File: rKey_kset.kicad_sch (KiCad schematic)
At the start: 25 parts, among them J1 Conn_01x08, Q1 BC337, Q2 BC337, Q3 BC337, Q4 BC337, Q5 BC337, Q6 BC337

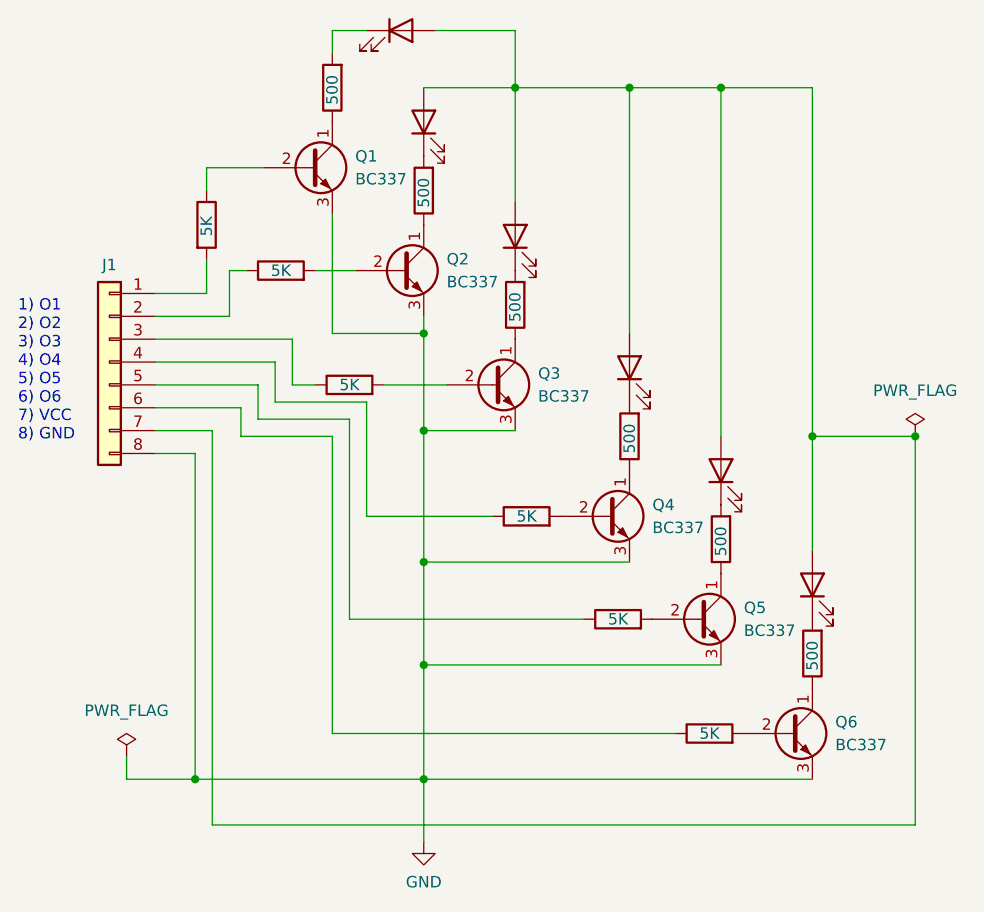
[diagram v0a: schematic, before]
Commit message: change: resistors values tuned to reduce the required current
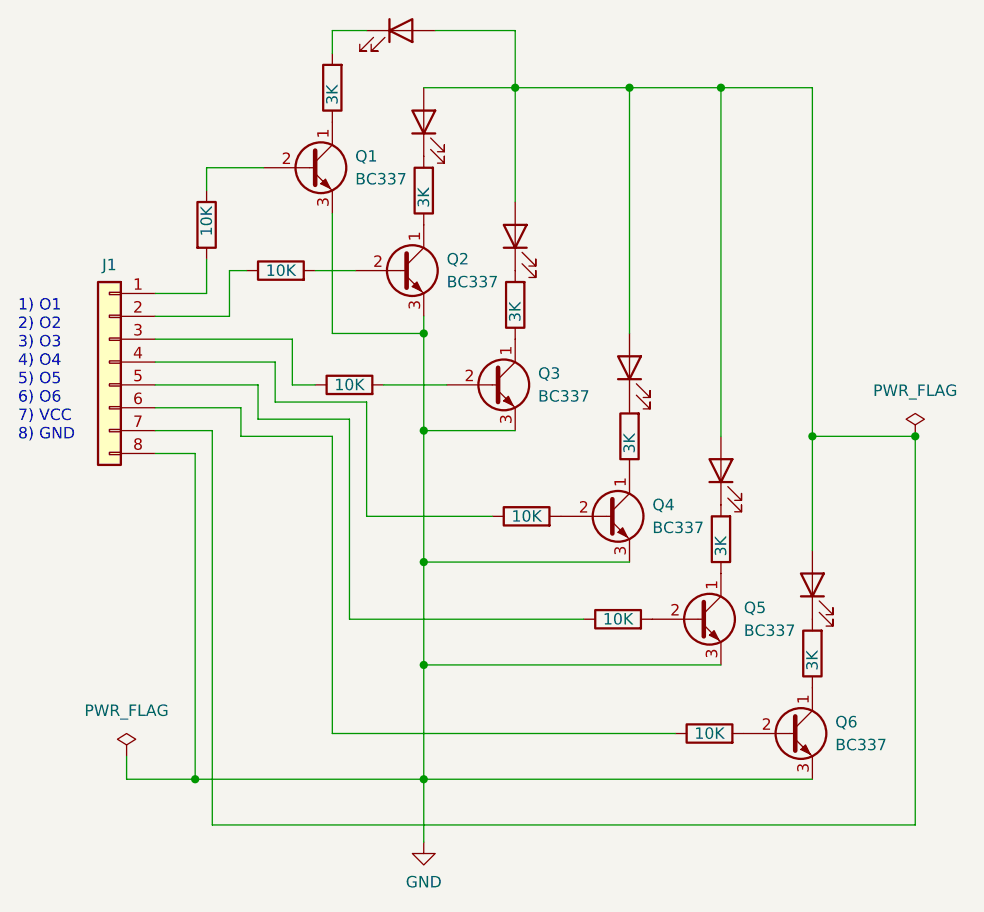
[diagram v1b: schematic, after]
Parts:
- R1, R10, R2, R4, R7, R8: value 5K -> 10K
- R11, R12, R3, R5, R6, R9: value 500 -> 3K
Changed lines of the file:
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@@
       (effects (font (size 1.27 1.27)) (justify right) hide)
     )
-    (property "Value" "500" (id 1) (at 160.655 114.3 90)
+    (property "Value" "3K" (id 1) (at 160.655 114.3 90)
       (effects (font (size 1.27 1.27)) (justify right))
     )
@@
       (effects (font (size 1.27 1.27)) (justify right) hide)
     )
-    (property "Value" "500" (id 1) (at 127.635 75.565 90)
+    (property "Value" "3K" (id 1) (at 127.635 75.565 90)
       (effects (font (size 1.27 1.27)) (justify right))
     )
@@
       (effects (font (size 1.27 1.27)) (justify right) hide)
     )
-    (property "Value" "500" (id 1) (at 117.475 62.865 90)
+    (property "Value" "3K" (id 1) (at 117.475 62.865 90)
       (effects (font (size 1.27 1.27)) (justify right))
     )
@@
       (effects (font (size 1.27 1.27)) hide)
     )
-    (property "Value" "5K" (id 1) (at 149.225 121.285 90))
+    (property "Value" "10K" (id 1) (at 149.225 121.285 90))
     (property "Footprint" "Resistor_THT:R_Axial_DIN0207_L6.3mm_D2.5mm_P7.62mm_Horizontal" (id 2) (at 149.225 123.063 90)
       (effects (font (size 1.27 1.27)) hide)
@@
       (effects (font (size 1.27 1.27)) (justify left) hide)
     )
-    (property "Value" "5K" (id 1) (at 93.345 66.04 90)
+    (property "Value" "10K" (id 1) (at 93.345 66.04 90)
       (effects (font (size 1.27 1.27)) (justify left))
     )
@@
       (effects (font (size 1.27 1.27)) (justify right) hide)
     )
-    (property "Value" "500" (id 1) (at 150.495 101.6 90)
+    (property "Value" "3K" (id 1) (at 150.495 101.6 90)
       (effects (font (size 1.27 1.27)) (justify right))
     )
@@
       (effects (font (size 1.27 1.27)) (justify right) hide)
     )
-    (property "Value" "500" (id 1) (at 140.335 90.17 90)
+    (property "Value" "3K" (id 1) (at 140.335 90.17 90)
       (effects (font (size 1.27 1.27)) (justify right))
     )
@@
       (effects (font (size 1.27 1.27)) hide)
     )
-    (property "Value" "5K" (id 1) (at 128.905 97.155 90))
+    (property "Value" "10K" (id 1) (at 128.905 97.155 90))
     (property "Footprint" "Resistor_THT:R_Axial_DIN0207_L6.3mm_D2.5mm_P7.62mm_Horizontal" (id 2) (at 128.905 98.933 90)
       (effects (font (size 1.27 1.27)) hide)
@@
       (effects (font (size 1.27 1.27)) hide)
     )
-    (property "Value" "5K" (id 1) (at 139.065 108.585 90))
+    (property "Value" "10K" (id 1) (at 139.065 108.585 90))
     (property "Footprint" "Resistor_THT:R_Axial_DIN0207_L6.3mm_D2.5mm_P7.62mm_Horizontal" (id 2) (at 139.065 110.363 90)
       (effects (font (size 1.27 1.27)) hide)
@@
       (effects (font (size 1.27 1.27)) (justify right) hide)
     )
-    (property "Value" "500" (id 1) (at 107.315 51.435 90)
+    (property "Value" "3K" (id 1) (at 107.315 51.435 90)
       (effects (font (size 1.27 1.27)) (justify right))
     )
@@
       (effects (font (size 1.27 1.27)) hide)
     )
-    (property "Value" "5K" (id 1) (at 109.22 82.55 90))
+    (property "Value" "10K" (id 1) (at 109.22 82.55 90))
     (property "Footprint" "Resistor_THT:R_Axial_DIN0207_L6.3mm_D2.5mm_P7.62mm_Horizontal" (id 2) (at 109.22 84.328 90)
       (effects (font (size 1.27 1.27)) hide)
@@
       (effects (font (size 1.27 1.27)) hide)
     )
-    (property "Value" "5K" (id 1) (at 101.6 69.85 90))
+    (property "Value" "10K" (id 1) (at 101.6 69.85 90))
     (property "Footprint" "Resistor_THT:R_Axial_DIN0207_L6.3mm_D2.5mm_P7.62mm_Horizontal" (id 2) (at 101.6 71.628 90)
       (effects (font (size 1.27 1.27)) hide)
@@
     )
     (path "/86766f6c-7782-457a-98bc-0ca91346751e"
-      (reference "R1") (unit 1) (value "5K") (footprint "Resistor_THT:R_Axial_DIN0207_L6.3mm_D2.5mm_P7.62mm_Horizontal")
+      (reference "R1") (unit 1) (value "10K") (footprint "Resistor_THT:R_Axial_DIN0207_L6.3mm_D2.5mm_P7.62mm_Horizontal")
     )
     (path "/fb958da6-9ccb-4c20-a5ac-1fd1757fff84"
-      (reference "R2") (unit 1) (value "5K") (footprint "Resistor_THT:R_Axial_DIN0207_L6.3mm_D2.5mm_P7.62mm_Horizontal")
+      (reference "R2") (unit 1) (value "10K") (footprint "Resistor_THT:R_Axial_DIN0207_L6.3mm_D2.5mm_P7.62mm_Horizontal")
     )
     (path "/ddbfa26a-ba5c-4563-b924-3bc3da5535c3"
-      (reference "R3") (unit 1) (value "500") (footprint "Resistor_THT:R_Axial_DIN0207_L6.3mm_D2.5mm_P7.62mm_Horizontal")
+      (reference "R3") (unit 1) (value "3K") (footprint "Resistor_THT:R_Axial_DIN0207_L6.3mm_D2.5mm_P7.62mm_Horizontal")
     )
     (path "/fa266512-6801-4085-8618-23c66236f734"
-      (reference "R4") (unit 1) (value "5K") (footprint "Resistor_THT:R_Axial_DIN0207_L6.3mm_D2.5mm_P7.62mm_Horizontal")
+      (reference "R4") (unit 1) (value "10K") (footprint "Resistor_THT:R_Axial_DIN0207_L6.3mm_D2.5mm_P7.62mm_Horizontal")
     )
     (path "/437219e0-6ddd-4812-8ea4-c8c01f1b8f2d"
-      (reference "R5") (unit 1) (value "500") (footprint "Resistor_THT:R_Axial_DIN0207_L6.3mm_D2.5mm_P7.62mm_Horizontal")
+      (reference "R5") (unit 1) (value "3K") (footprint "Resistor_THT:R_Axial_DIN0207_L6.3mm_D2.5mm_P7.62mm_Horizontal")
     )
     (path "/35747f08-c664-4fc0-b874-edb7c22b63e6"
-      (reference "R6") (unit 1) (value "500") (footprint "Resistor_THT:R_Axial_DIN0207_L6.3mm_D2.5mm_P7.62mm_Horizontal")
+      (reference "R6") (unit 1) (value "3K") (footprint "Resistor_THT:R_Axial_DIN0207_L6.3mm_D2.5mm_P7.62mm_Horizontal")
     )
     (path "/a2319e72-4d24-41ef-b06d-79a861ef557a"
-      (reference "R7") (unit 1) (value "5K") (footprint "Resistor_THT:R_Axial_DIN0207_L6.3mm_D2.5mm_P7.62mm_Horizontal")
+      (reference "R7") (unit 1) (value "10K") (footprint "Resistor_THT:R_Axial_DIN0207_L6.3mm_D2.5mm_P7.62mm_Horizontal")
     )
     (path "/cdecf091-b947-4796-8510-ea73a1b2a01b"
-      (reference "R8") (unit 1) (value "5K") (footprint "Resistor_THT:R_Axial_DIN0207_L6.3mm_D2.5mm_P7.62mm_Horizontal")
+      (reference "R8") (unit 1) (value "10K") (footprint "Resistor_THT:R_Axial_DIN0207_L6.3mm_D2.5mm_P7.62mm_Horizontal")
     )
     (path "/9ef8560a-564c-414c-9ae1-bb7360b1bf4b"
-      (reference "R9") (unit 1) (value "500") (footprint "Resistor_THT:R_Axial_DIN0207_L6.3mm_D2.5mm_P7.62mm_Horizontal")
+      (reference "R9") (unit 1) (value "3K") (footprint "Resistor_THT:R_Axial_DIN0207_L6.3mm_D2.5mm_P7.62mm_Horizontal")
     )
     (path "/5daad55e-0b78-4a14-a8ef-920ac71c8708"
-      (reference "R10") (unit 1) (value "5K") (footprint "Resistor_THT:R_Axial_DIN0207_L6.3mm_D2.5mm_P7.62mm_Horizontal")
+      (reference "R10") (unit 1) (value "10K") (footprint "Resistor_THT:R_Axial_DIN0207_L6.3mm_D2.5mm_P7.62mm_Horizontal")
     )
     (path "/90aa192d-321d-4553-babc-f4088cfca1f6"
-      (reference "R11") (unit 1) (value "500") (footprint "Resistor_THT:R_Axial_DIN0207_L6.3mm_D2.5mm_P7.62mm_Horizontal")
+      (reference "R11") (unit 1) (value "3K") (footprint "Resistor_THT:R_Axial_DIN0207_L6.3mm_D2.5mm_P7.62mm_Horizontal")
     )
     (path "/32a96ef3-5e5b-4cdd-9c41-6b27a92b77ef"
-      (reference "R12") (unit 1) (value "500") (footprint "Resistor_THT:R_Axial_DIN0207_L6.3mm_D2.5mm_P7.62mm_Horizontal")
-    )
-  )
+      (reference "R12") (unit 1) (value "3K") (footprint "Resistor_THT:R_Axial_DIN0207_L6.3mm_D2.5mm_P7.62mm_Horizontal")
+    )
+  )
